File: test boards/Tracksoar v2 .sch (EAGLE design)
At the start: 40 parts, among them IC1 BME280, IC2 74AHC1G125DBV, Y1 16MHZ

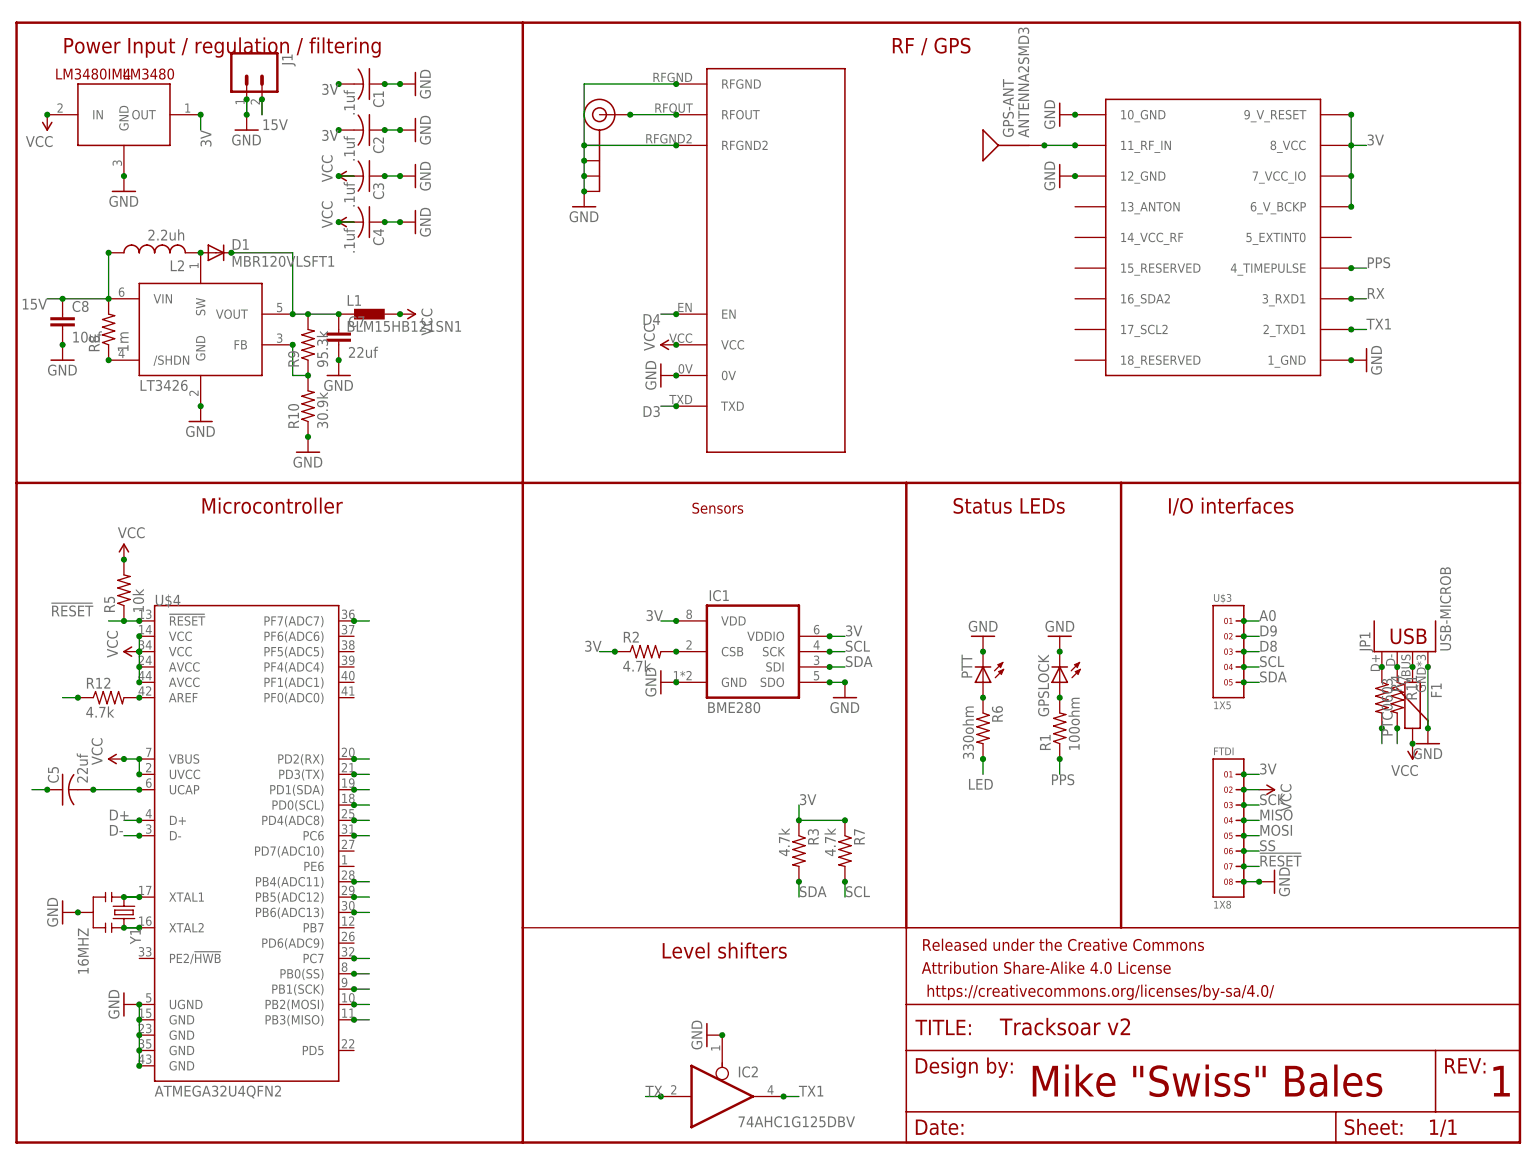
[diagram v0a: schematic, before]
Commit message: tracksoar v2 rev 5
converted to 4 layer board, covered via with solder mask, routed vcc
and gnd on internal planes. Corrected AREF connection to ground via
cap. Added analog pin connection to 15v to measure battery voltage.
General routing cleanup.
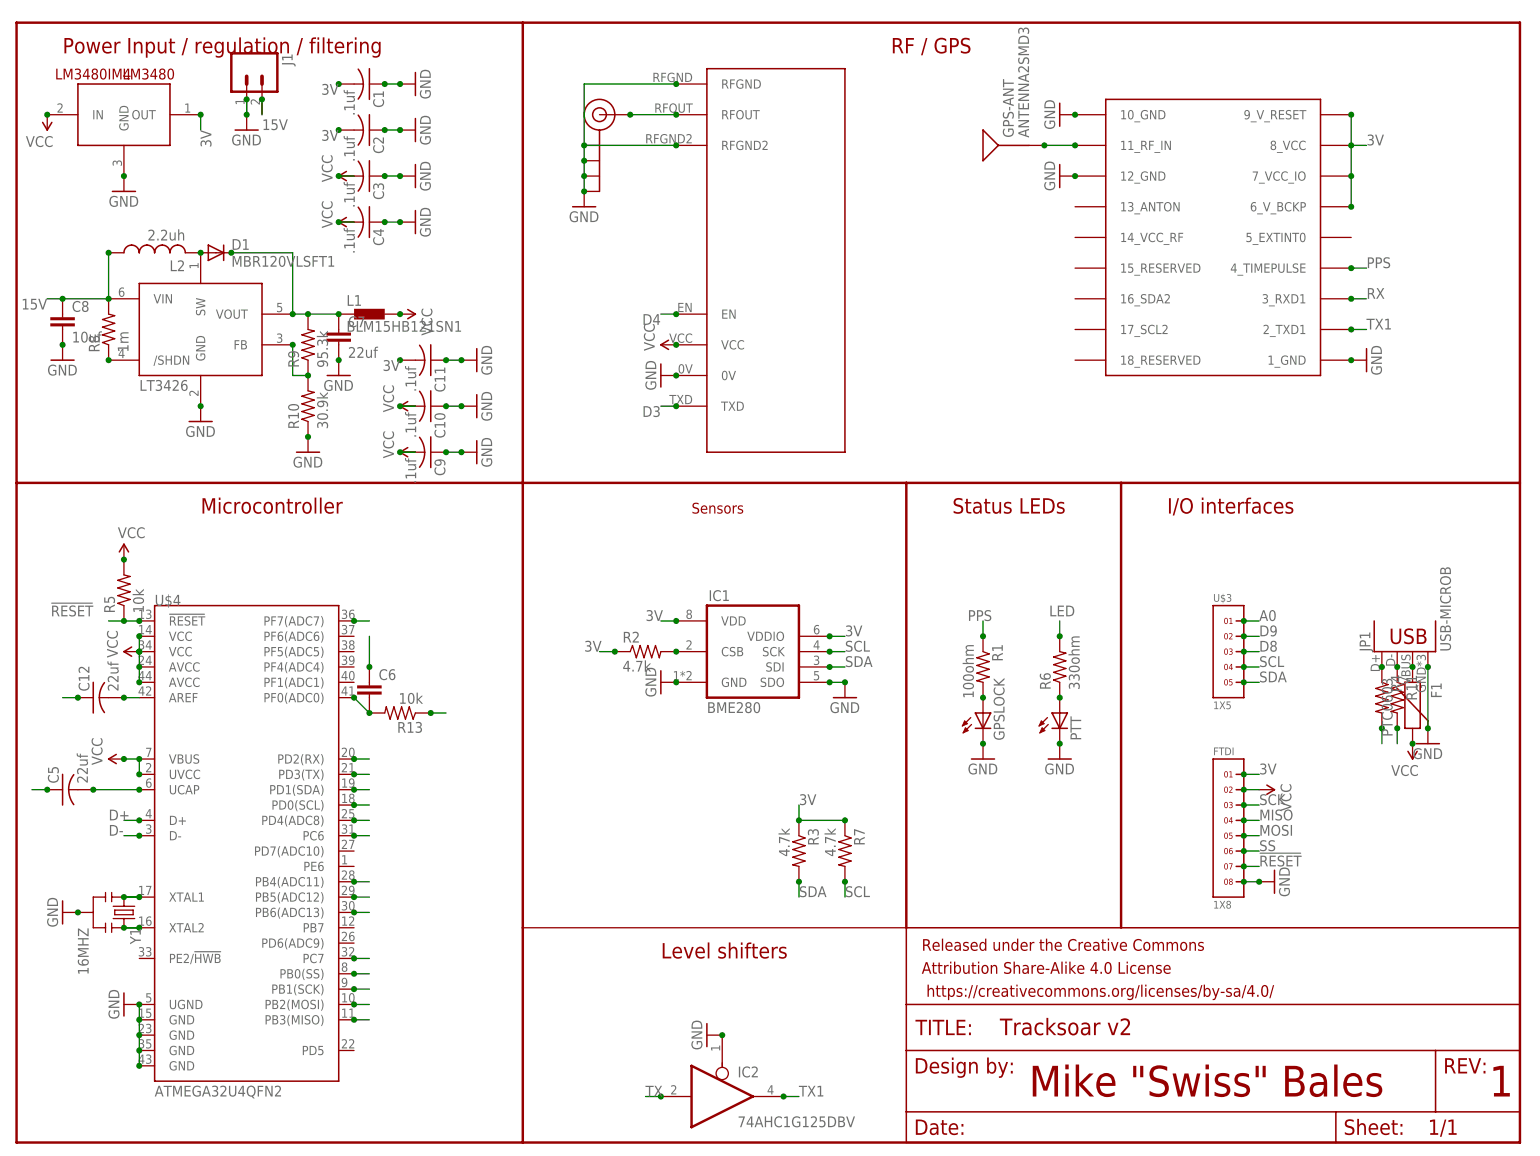
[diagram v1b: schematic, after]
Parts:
- removed R12: 4.7k, adafruit:R-US_R0402
- added C10, C11, C9: .1uf, adafruit:C-USC0402
- added C12: 22uf, rcl:C-USC0402
- added C6: (no value), SparkFun-Passives:CAP0402-CAP
- added R13: 10k, adafruit:R-US_R0402
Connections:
- new net N$21: C6.2, R13.2, U$4.PF0(ADC0)
- net 15V: now also R13.1; no longer R12.1
- net 3V: now also C11.2
- net GND: now also C10.1, C11.1, C12.1, C6.1, C9.1
- net N$17: now also C12.2; no longer R12.2
- net VCC: now also C10.2, C9.2
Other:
- moved on the sheet: GPSLOCK, PTT, R1, R6
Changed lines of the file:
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@@
 <part name="C5" library="rcl" deviceset="C-US" device="C0402" value="22uf"/>
 <part name="U$3" library="headers(2mm)" deviceset="1X5" device=""/>
-<part name="R12" library="adafruit" deviceset="R-US_" device="R0402" value="4.7k"/>
 <part name="L1" library="inductors" deviceset="BLM15H" device="" technology="B121SN1"/>
+<part name="R13" library="adafruit" deviceset="R-US_" device="R0402" value="10k"/>
+<part name="C6" library="SparkFun-Passives" deviceset="CAP" device="0402-CAP"/>
+<part name="C9" library="adafruit" deviceset="C-US" device="C0402" value=".1uf"/>
+<part name="GND10" library="SparkFun-Aesthetics" deviceset="GND" device=""/>
+<part name="SUPPLY7" library="SparkFun-Aesthetics" deviceset="VCC" device=""/>
+<part name="C10" library="adafruit" deviceset="C-US" device="C0402" value=".1uf"/>
+<part name="GND12" library="SparkFun-Aesthetics" deviceset="GND" device=""/>
+<part name="SUPPLY8" library="SparkFun-Aesthetics" deviceset="VCC" device=""/>
+<part name="C11" library="adafruit" deviceset="C-US" device="C0402" value=".1uf"/>
+<part name="GND16" library="SparkFun-Aesthetics" deviceset="GND" device=""/>
+<part name="C12" library="rcl" deviceset="C-US" device="C0402" value="22uf"/>
 </parts>
 <sheets>
@@
 <instance part="SUPPLY3" gate="G$1" x="109.22" y="132.08" rot="R90"/>
 <instance part="GND7" gate="1" x="106.68" y="127" rot="R270"/>
-<instance part="R1" gate="G$1" x="172.72" y="68.58" rot="R90"/>
-<instance part="GPSLOCK" gate="G$1" x="172.72" y="76.2" rot="R180"/>
-<instance part="GND8" gate="1" x="172.72" y="83.82" rot="R180"/>
+<instance part="R1" gate="G$1" x="160.02" y="78.74" rot="R270"/>
+<instance part="GPSLOCK" gate="G$1" x="160.02" y="71.12"/>
+<instance part="GND8" gate="1" x="160.02" y="63.5"/>
 <instance part="GND9" gate="1" x="223.52" y="129.54" rot="R90"/>
 <instance part="GND13" gate="1" x="172.72" y="160.02" rot="R270"/>
@@
 <instance part="FRAME1" gate="G$1" x="0" y="0"/>
 <instance part="FRAME1" gate="G$2" x="147.32" y="0"/>
-<instance part="PTT" gate="G$1" x="160.02" y="76.2" rot="R180"/>
-<instance part="R6" gate="G$1" x="160.02" y="68.58" rot="R270"/>
-<instance part="GND26" gate="1" x="160.02" y="83.82" rot="R180"/>
+<instance part="PTT" gate="G$1" x="172.72" y="71.12"/>
+<instance part="R6" gate="G$1" x="172.72" y="78.74" rot="R90"/>
+<instance part="GND26" gate="1" x="172.72" y="63.5"/>
 <instance part="GND24" gate="1" x="7.62" y="38.1" rot="R270"/>
 <instance part="Y1" gate="G$1" x="17.78" y="38.1" rot="R270"/>
@@
 <instance part="C5" gate="G$1" x="7.62" y="58.42" rot="R90"/>
 <instance part="U$3" gate="G$1" x="200.66" y="81.28"/>
-<instance part="R12" gate="G$1" x="15.24" y="73.66"/>
 <instance part="L1" gate="G$1" x="58.42" y="137.16"/>
+<instance part="R13" gate="G$1" x="63.5" y="71.12" rot="R180"/>
+<instance part="C6" gate="G$1" x="58.42" y="73.66"/>
+<instance part="C9" gate="G$1" x="68.58" y="114.3" rot="R270"/>
+<instance part="GND10" gate="1" x="76.2" y="114.3" rot="R90"/>
+<instance part="SUPPLY7" gate="G$1" x="66.04" y="114.3" rot="R90"/>
+<instance part="C10" gate="G$1" x="68.58" y="121.92" rot="R270"/>
+<instance part="GND12" gate="1" x="76.2" y="121.92" rot="R90"/>
+<instance part="SUPPLY8" gate="G$1" x="66.04" y="121.92" rot="R90"/>
+<instance part="C11" gate="G$1" x="68.58" y="129.54" rot="R270"/>
+<instance part="GND16" gate="1" x="76.2" y="129.54" rot="R90"/>
+<instance part="C12" gate="G$1" x="12.7" y="73.66" rot="R90"/>
 </instances>
 <busses>
@@
 <pinref part="GPSLOCK" gate="G$1" pin="C"/>
 <pinref part="GND8" gate="1" pin="GND"/>
-<junction x="172.72" y="81.28"/>
+<junction x="160.02" y="66.04"/>
 </segment>
 <segment>
@@
 <pinref part="PTT" gate="G$1" pin="C"/>
 <pinref part="GND26" gate="1" pin="GND"/>
-<junction x="160.02" y="81.28"/>
+<junction x="172.72" y="66.04"/>
 </segment>
 <segment>
@@
 <junction x="5.08" y="58.42"/>
 </segment>
+<segment>
+<wire x1="58.42" y1="78.74" x2="58.42" y2="83.82" width="0.1524" layer="91"/>
+<pinref part="C6" gate="G$1" pin="1"/>
+<junction x="58.42" y="78.74"/>
+</segment>
+<segment>
+<pinref part="C9" gate="G$1" pin="1"/>
+<pinref part="GND10" gate="1" pin="GND"/>
+<junction x="71.12" y="114.3"/>
+<wire x1="73.66" y1="114.3" x2="71.12" y2="114.3" width="0.1524" layer="91"/>
+<junction x="73.66" y="114.3"/>
+</segment>
+<segment>
+<pinref part="C10" gate="G$1" pin="1"/>
+<pinref part="GND12" gate="1" pin="GND"/>
+<junction x="71.12" y="121.92"/>
+<wire x1="73.66" y1="121.92" x2="71.12" y2="121.92" width="0.1524" layer="91"/>
+<junction x="73.66" y="121.92"/>
+</segment>
+<segment>
+<pinref part="C11" gate="G$1" pin="1"/>
+<pinref part="GND16" gate="1" pin="GND"/>
+<junction x="71.12" y="129.54"/>
+<wire x1="73.66" y1="129.54" x2="71.12" y2="129.54" width="0.1524" layer="91"/>
+<junction x="73.66" y="129.54"/>
+</segment>
+<segment>
+<wire x1="10.16" y1="73.66" x2="7.62" y2="73.66" width="0.1524" layer="91"/>
+<pinref part="C12" gate="G$1" pin="1"/>
+<junction x="10.16" y="73.66"/>
+</segment>
 </net>
 <net name="D3" class="0">
@@
 <junction x="63.5" y="137.16"/>
 </segment>
+<segment>
+<pinref part="C9" gate="G$1" pin="2"/>
+<pinref part="SUPPLY7" gate="G$1" pin="VCC"/>
+<junction x="63.5" y="114.3"/>
+<wire x1="66.04" y1="114.3" x2="63.5" y2="114.3" width="0.1524" layer="91"/>
+</segment>
+<segment>
+<pinref part="C10" gate="G$1" pin="2"/>
+<pinref part="SUPPLY8" gate="G$1" pin="VCC"/>
+<junction x="63.5" y="121.92"/>
+<wire x1="66.04" y1="121.92" x2="63.5" y2="121.92" width="0.1524" layer="91"/>
+</segment>
 </net>
 <net name="3V" class="0">
@@
 <label x="205.74" y="60.96" size="1.778" layer="95"/>
 </segment>
+<segment>
+<pinref part="C11" gate="G$1" pin="2"/>
+<label x="63.5" y="129.54" size="1.778" layer="95" rot="R180"/>
+<junction x="63.5" y="129.54"/>
+</segment>
 </net>
 <net name="N$1" class="0">
@@
 <pinref part="R1" gate="G$1" pin="2"/>
 <pinref part="GPSLOCK" gate="G$1" pin="A"/>
-<junction x="172.72" y="73.66"/>
+<junction x="160.02" y="73.66"/>
 </segment>
 </net>
@@
 <pinref part="PTT" gate="G$1" pin="A"/>
 <pinref part="R6" gate="G$1" pin="1"/>
-<junction x="160.02" y="73.66"/>
+<junction x="172.72" y="73.66"/>
 </segment>
 </net>
@@
 <segment>
 <pinref part="R6" gate="G$1" pin="2"/>
-<wire x1="160.02" y1="63.5" x2="160.02" y2="60.96" width="0.1524" layer="91"/>
-<label x="157.48" y="58.42" size="1.778" layer="95"/>
-<junction x="160.02" y="63.5"/>
+<wire x1="172.72" y1="83.82" x2="172.72" y2="86.36" width="0.1524" layer="91"/>
+<label x="175.26" y="88.9" size="1.778" layer="95" rot="R180"/>
+<junction x="172.72" y="83.82"/>
 </segment>
 <segment>
@@
 </segment>
 <segment>
-<pinref part="R12" gate="G$1" pin="1"/>
-<wire x1="10.16" y1="73.66" x2="7.62" y2="73.66" width="0.1524" layer="91"/>
-<junction x="10.16" y="73.66"/>
+<pinref part="R13" gate="G$1" pin="1"/>
+<wire x1="68.58" y1="71.12" x2="71.12" y2="71.12" width="0.1524" layer="91"/>
+<junction x="68.58" y="71.12"/>
 </segment>
 </net>
@@
 <segment>
 <pinref part="R1" gate="G$1" pin="1"/>
-<wire x1="172.72" y1="63.5" x2="172.72" y2="60.96" width="0.1524" layer="91"/>
-<junction x="172.72" y="63.5"/>
-<label x="175.26" y="60.96" size="1.778" layer="95" rot="R180"/>
+<wire x1="160.02" y1="83.82" x2="160.02" y2="86.36" width="0.1524" layer="91"/>
+<junction x="160.02" y="83.82"/>
+<label x="157.48" y="86.36" size="1.778" layer="95"/>
 </segment>
 </net>
@@
 <junction x="203.2" y="86.36"/>
 <label x="205.74" y="86.36" size="1.778" layer="95"/>
-</segment>
-</net>
-<net name="N$17" class="0">
-<segment>
-<pinref part="U$4" gate="G$1" pin="AREF"/>
-<pinref part="R12" gate="G$1" pin="2"/>
-<junction x="20.32" y="73.66"/>
 </segment>
 </net>
@@
 </segment>
 </net>
+<net name="N$21" class="0">
+<segment>
+<pinref part="U$4" gate="G$1" pin="PF0(ADC0)"/>
+<wire x1="58.42" y1="71.12" x2="55.88" y2="73.66" width="0.1524" layer="91"/>
+<junction x="55.88" y="73.66"/>
+<pinref part="R13" gate="G$1" pin="2"/>
+<junction x="58.42" y="71.12"/>
+<pinref part="C6" gate="G$1" pin="2"/>
+</segment>
+</net>
+<net name="N$17" class="0">
+<segment>
+<pinref part="U$4" gate="G$1" pin="AREF"/>
+<pinref part="C12" gate="G$1" pin="2"/>
+<wire x1="17.78" y1="73.66" x2="20.32" y2="73.66" width="0.1524" layer="91"/>
+<junction x="17.78" y="73.66"/>
+</segment>
+</net>

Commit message: Updated Silkscreen
Updated capacitor values and schematic symbols. Updated silkscreen to
remove overlaps and standardized text size.
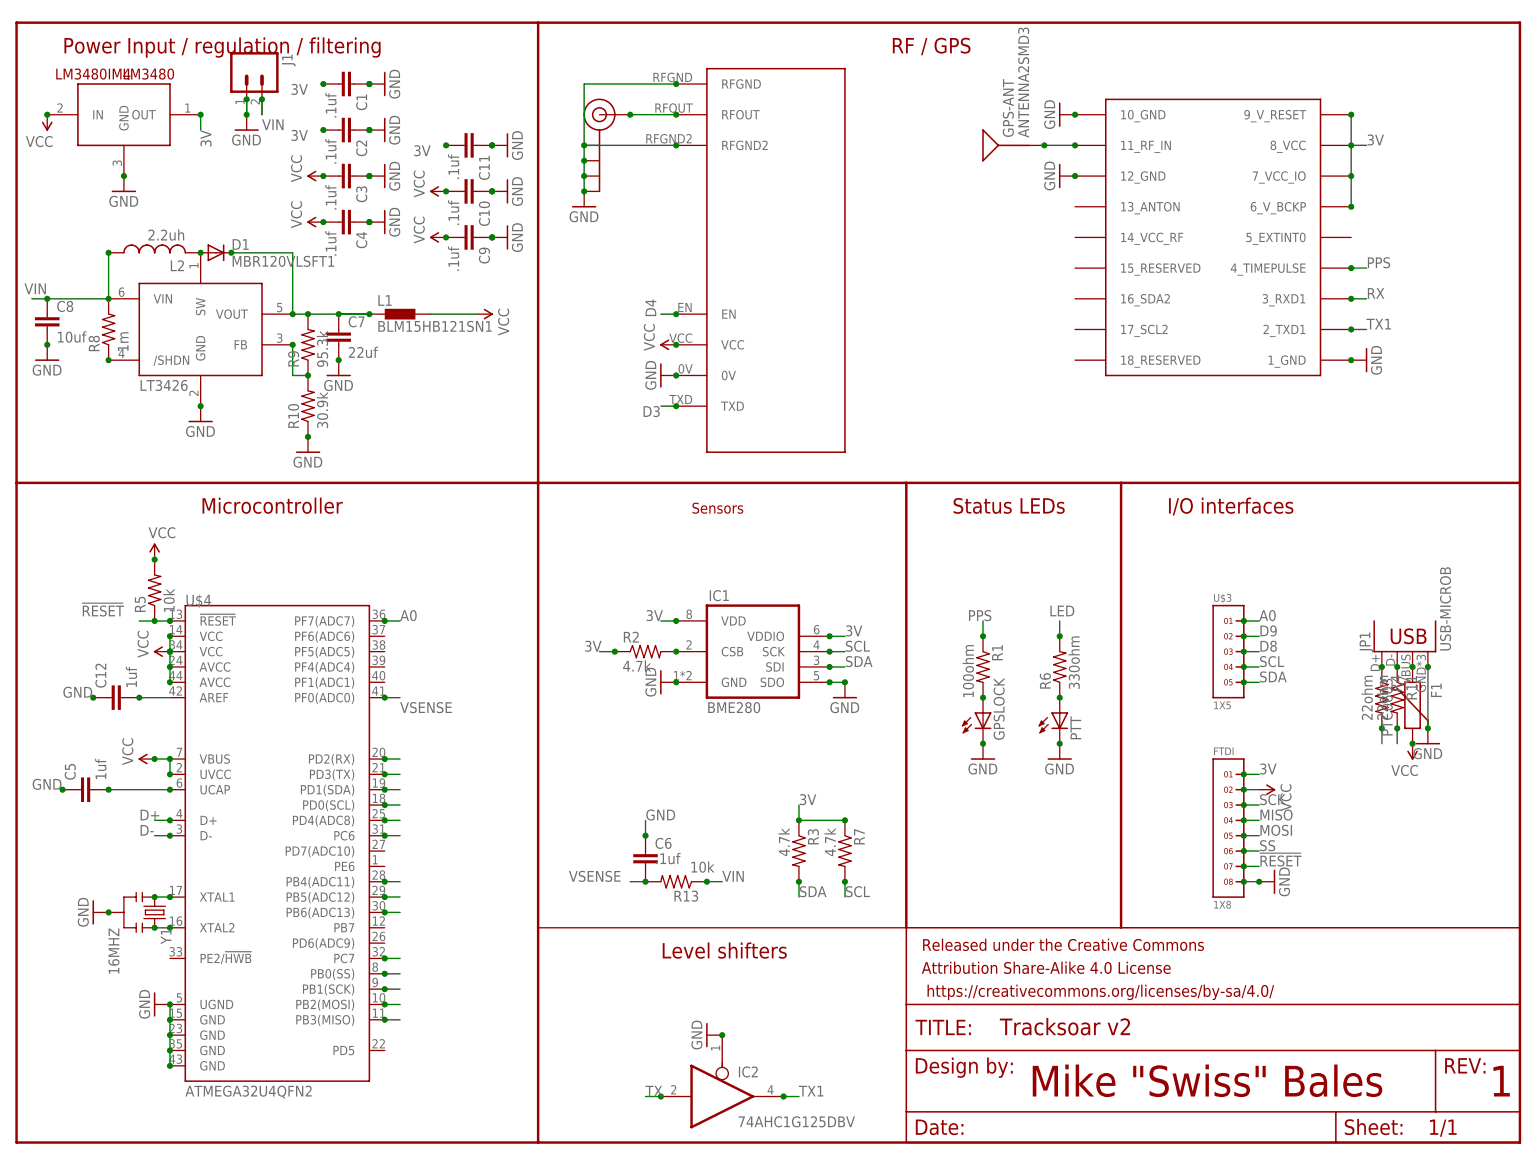
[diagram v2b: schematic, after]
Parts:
- C1, C10, C11, C2, C3, C4, C9: device adafruit:C-USC0402 -> SparkFun-Capacitors:CAP0402-CAP
- C12, C5: value 22uf -> 1uf; device rcl:C-USC0402 -> SparkFun-Capacitors:CAP0402-CAP
- C6: value (none) -> .1uf
- R11, R4: value (none) -> 22ohm
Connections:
- net 15V renamed VIN
- net N$21 renamed VSENSE
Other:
- moved on the sheet: C1, C10, C11, C12, C2, C3, C4, C5, C6, C8, C9, L1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
